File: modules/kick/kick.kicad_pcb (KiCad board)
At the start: 2 copper layers, 30.5 x 68.6 mm, 4 parts

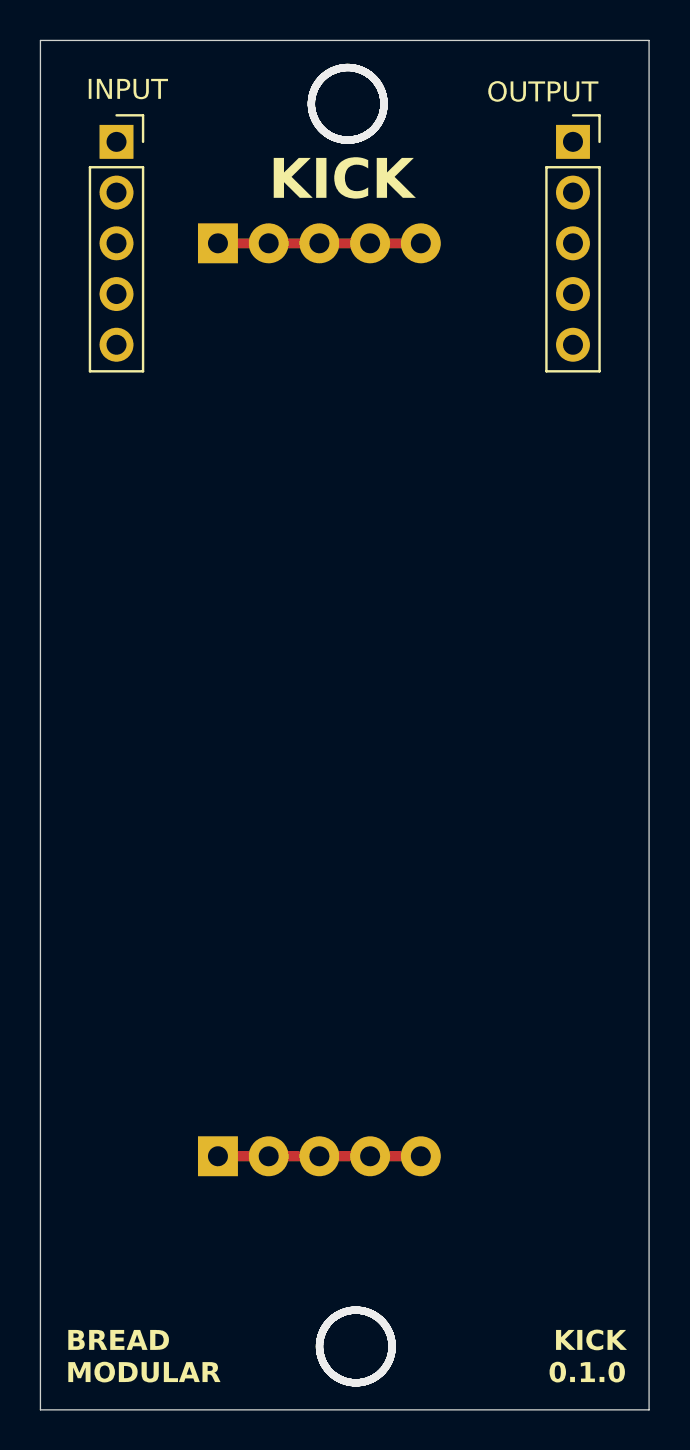
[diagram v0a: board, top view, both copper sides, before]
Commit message: Finished the 4 layer board.
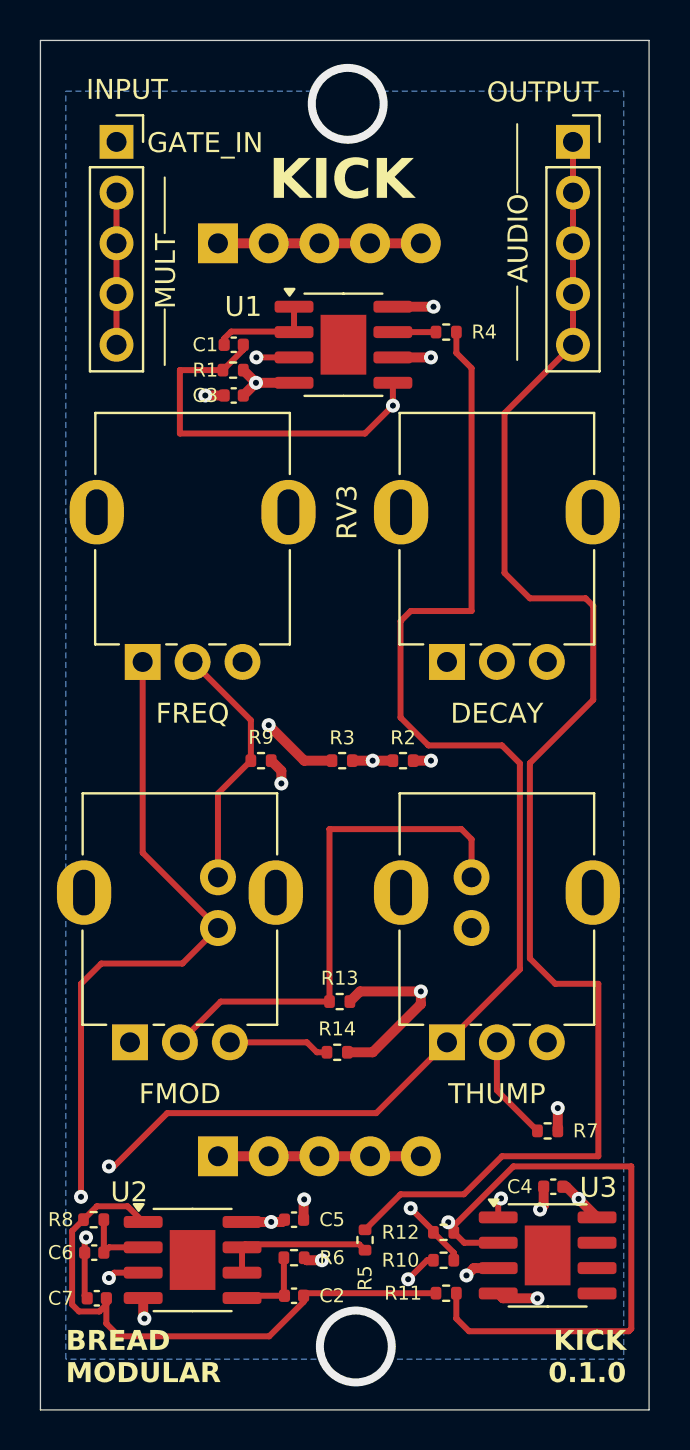
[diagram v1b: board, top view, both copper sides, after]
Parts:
- added C1: 100nf, Capacitor_SMD:C_0402_1005Metric, F.Cu at (56.7, 55.9)
- added C2: 100nf, Capacitor_SMD:C_0402_1005Metric, F.Cu at (59.7, 103.5)
- added C3: 100nf, Capacitor_SMD:C_0402_1005Metric, F.Cu at (56.7, 58.4)
- added C4: 100nf, Capacitor_SMD:C_0402_1005Metric, F.Cu at (72.7, 98.0)
- added C5: 100nf, Capacitor_SMD:C_0402_1005Metric, F.Cu at (59.7, 99.7)
- added C6: 10nf, Capacitor_SMD:C_0402_1005Metric, F.Cu at (49.7, 101.3)
- added C7: 10nf, Capacitor_SMD:C_0402_1005Metric, F.Cu at (49.8, 103.6)
- added R1: 51k, Resistor_SMD:R_0402_1005Metric, F.Cu at (56.6, 57.1)
- added R10: 470k, Resistor_SMD:R_0402_1005Metric, F.Cu at (67.2, 101.7)
- added R11: 100k, Resistor_SMD:R_0402_1005Metric, F.Cu at (67.3, 103.4)
- added R12: 100k, Resistor_SMD:R_0402_1005Metric, F.Cu at (67.2, 100.3)
- added R13: 200k, Resistor_SMD:R_0402_1005Metric, F.Cu at (62.0, 88.8)
- added R14: 10k, Resistor_SMD:R_0402_1005Metric, F.Cu at (61.9, 91.3)
- added R2: 1k, Resistor_SMD:R_0402_1005Metric, F.Cu at (65.1, 76.7)
- added R3: 1k, Resistor_SMD:R_0402_1005Metric, F.Cu at (62.1, 76.7)
- added R4: 100k, Resistor_SMD:R_0402_1005Metric, F.Cu at (67.3, 55.2)
- added R5: 1k, Resistor_SMD:R_0402_1005Metric, F.Cu at (63.2, 100.7)
- added R6: 1M, Resistor_SMD:R_0402_1005Metric, F.Cu at (59.7, 101.6)
- added R7: 1k, Resistor_SMD:R_0402_1005Metric, F.Cu at (72.4, 95.2)
- added R8: 1M, Resistor_SMD:R_0402_1005Metric, F.Cu at (49.7, 99.7)
- added R9: 4.7k, Resistor_SMD:R_0402_1005Metric, F.Cu at (58.0, 76.7)
- added RV1: 50k, BreadModular_Pots:Potentiometer_RV09, F.Cu at (67.3, 90.8)
- added RV2: 1M, BreadModular_Pots:Potentiometer_RV09, F.Cu at (52.1, 71.8)
- added RV3: 1M, BreadModular_Pots:Potentiometer_RV09, F.Cu at (67.3, 71.8)
- added RV4: 1M, BreadModular_Pots:Potentiometer_RV09, F.Cu at (51.5, 90.8)
- added U1: MCP6002-xSN, Package_SO:SOIC-8-1EP_3.9x4.9mm_P1.27mm_EP2.29x3mm, F.Cu at (62.2, 55.9)
- added U2: MCP6002-xSN, Package_SO:SOIC-8-1EP_3.9x4.9mm_P1.27mm_EP2.29x3mm, F.Cu at (54.6, 101.7)
- added U3: MCP6002-xSN, Package_SO:SOIC-8-1EP_3.9x4.9mm_P1.27mm_EP2.29x3mm, F.Cu at (72.4, 101.5)
- added U4: VTL5C, BreadModular_MISC:VTL5C, B.Cu at (62.2, 83.8)
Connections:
- INPUT1 pad 1: unconnected-(INPUT1-Pin_1-Pad1) -> GATE_IN
- INPUT1 pad 2: unconnected-(INPUT1-Pin_2-Pad2) -> Net-(INPUT1-Pin_2)
- INPUT1 pad 3: unconnected-(INPUT1-Pin_3-Pad3) -> Net-(INPUT1-Pin_2)
- INPUT1 pad 4: unconnected-(INPUT1-Pin_4-Pad4) -> Net-(INPUT1-Pin_2)
- INPUT1 pad 5: unconnected-(INPUT1-Pin_5-Pad5) -> Net-(INPUT1-Pin_2)
- OUTPUT1 pad 1: unconnected-(OUTPUT1-Pin_1-Pad1) -> KICK_OUT
- OUTPUT1 pad 2: unconnected-(OUTPUT1-Pin_2-Pad2) -> KICK_OUT
- OUTPUT1 pad 3: unconnected-(OUTPUT1-Pin_3-Pad3) -> KICK_OUT
- OUTPUT1 pad 4: unconnected-(OUTPUT1-Pin_4-Pad4) -> KICK_OUT
- OUTPUT1 pad 5: unconnected-(OUTPUT1-Pin_5-Pad5) -> KICK_OUT
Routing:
- net V_MID: track 0.00 -> 119.8 mm, vias 0 -> 6
- net Net-(U3A--): track 0.00 -> 97.3 mm, vias 0 -> 1
- net Net-(R10-Pad1): track 0.00 -> 73.8 mm, vias 0 -> 2
- net KICK_OUT: track 0.00 -> 72.9 mm
- net Net-(U2A-+): track 0.00 -> 72.2 mm, vias 0 -> 2
- net CAP_MID: track 0.00 -> 59.6 mm, vias 0 -> 3
- net TRIG_ENV: track 0.00 -> 52.7 mm, vias 0 -> 1
- net SHAPE_OUT: track 0.00 -> 29.5 mm
- net Net-(U4--): track 0.00 -> 26.2 mm
- net GND: track 10.2 -> 32.2 mm, vias 0 -> 7
- net GATE_IN: track 0.00 -> 17.8 mm, vias 0 -> 1
- net Net-(R9-Pad1): track 0.00 -> 12.7 mm
- net V_SUPPLY: track 10.2 -> 18.6 mm, vias 0 -> 5
- net Net-(INPUT1-Pin_2): track 0.00 -> 7.62 mm
- net Net-(U2B--): track 0.00 -> 7.61 mm
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- added copper zone on B.Cu, net GND
- added copper zone on In1.Cu, net V_MID
- added copper zone on In2.Cu, net V_SUPPLY
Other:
- copper layers 2 -> 4
- board text added: "AUDIO"
- board text added: "DECAY"
- board text added: "FMOD"
- board text added: "FREQ"
- board text added: "GATE_IN"
- board text added: "MULT"
- board text added: "THUMP"

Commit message: Add production files.
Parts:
- added R15: 200k, Resistor_SMD:R_0402_1005Metric, F.Cu at (66.8, 101.9)
- added R16: 51k, Resistor_SMD:R_0402_1005Metric, F.Cu at (66.8, 102.9)
- R10: value 470k -> 200k
- moved C2 4.30 mm to (55.7, 105.2)
- moved R11 3.03 mm to (69.8, 105.0)
- moved R10 0.97 mm to (66.8, 100.8)
- moved R12 0.91 mm to (66.7, 99.6)
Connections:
- R10 pad 2: CAP_MID -> Net-(R10-Pad2)
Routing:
- net SHAPE_OUT: track 29.5 -> 33.2 mm
- net Net-(U2B-+): track 4.09 -> 6.28 mm
- net Net-(R10-Pad1): track 73.8 -> 72.5 mm
- net Net-(R15-Pad2): track 0.00 -> 1.02 mm
- net Net-(R10-Pad2): track 0.00 -> 1.02 mm
- net KICK_OUT: track 72.9 -> 73.8 mm
